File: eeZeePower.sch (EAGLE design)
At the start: 11 parts

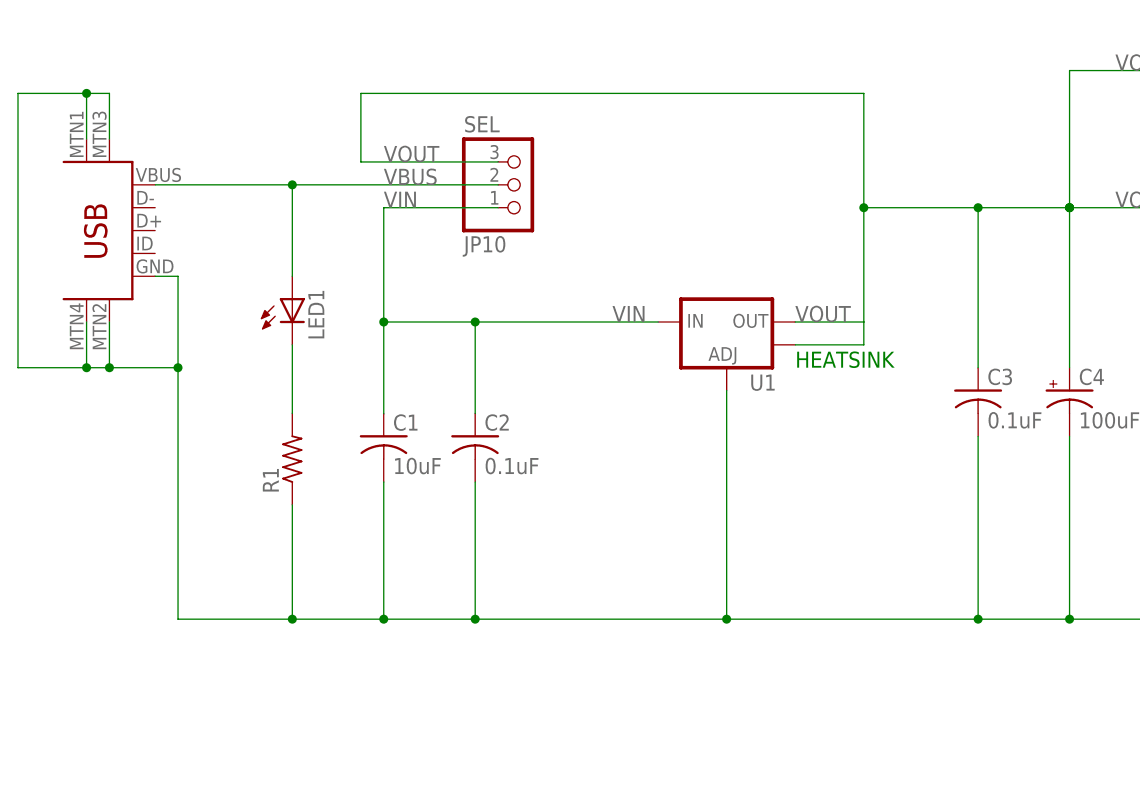
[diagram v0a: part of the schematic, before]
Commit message: Switched to TC1262 regulator, improved thermal design, moved jumper and LED around.
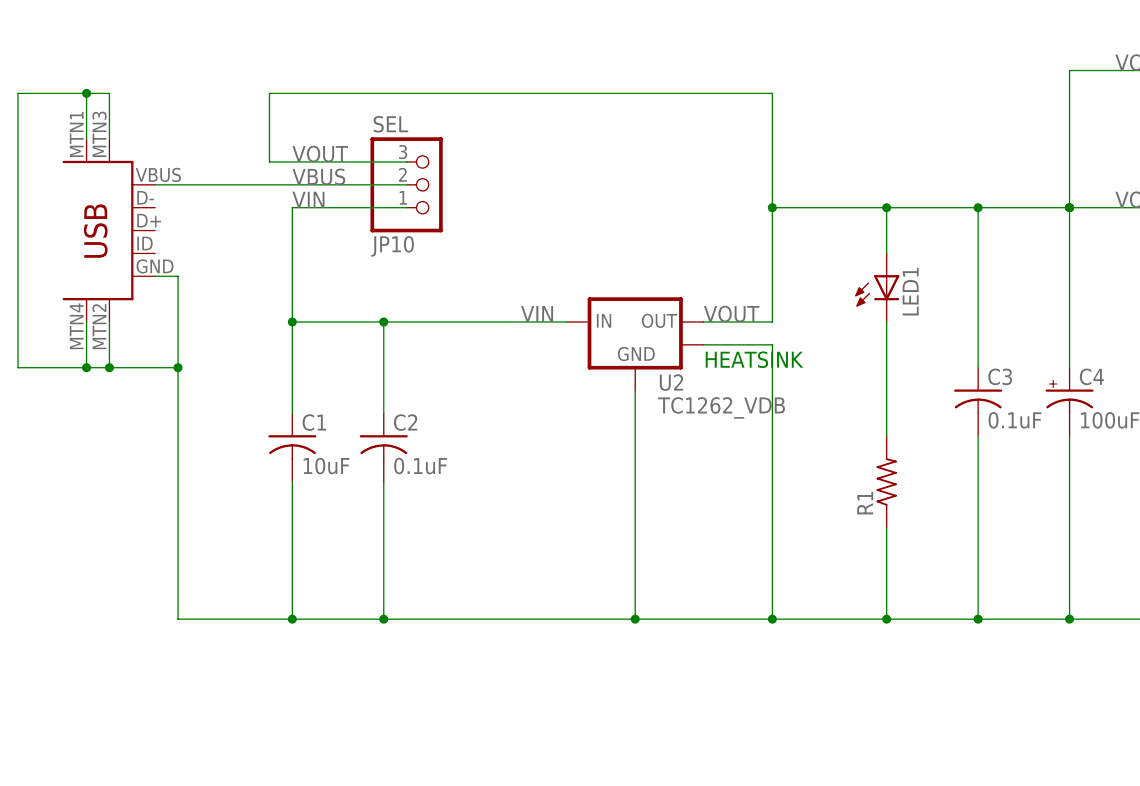
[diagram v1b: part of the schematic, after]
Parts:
- removed U1: (no value), SparkFun:V_REG_LM1117SOT223
- added U2: TC1262_VDB, bt_regulator:TC1262_VDB
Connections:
- net GND: now also U2.GND, U2.TAB; no longer U1.ADJ
- net VBUS: no longer LED1.A
- net VIN: now also U2.VIN; no longer U1.IN
- net VOUT: now also LED1.A, U2.VOUT; no longer U1.OUT, U1.OUT@1
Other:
- moved on the sheet: C1, C2, JP10, LED1, R1
